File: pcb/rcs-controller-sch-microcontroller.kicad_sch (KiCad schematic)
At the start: 42 parts, among them J11 Conn_01x03, J4 Screw_Terminal_4_P3.50mm, J5 USB_C_Receptacle_USB2.0_14P, J6 Conn_01x03, J9 Conn_01x03, Q2 SI7465DP-T1-E3, Q3 SI7465DP-T1-E3, Q4 PMV45EN2, Q5 PMV45EN2, SW1 SW_Push, SW2 SW_Push, U1 LSM6DSOX, U4 ESP32-S3-WROOM-1

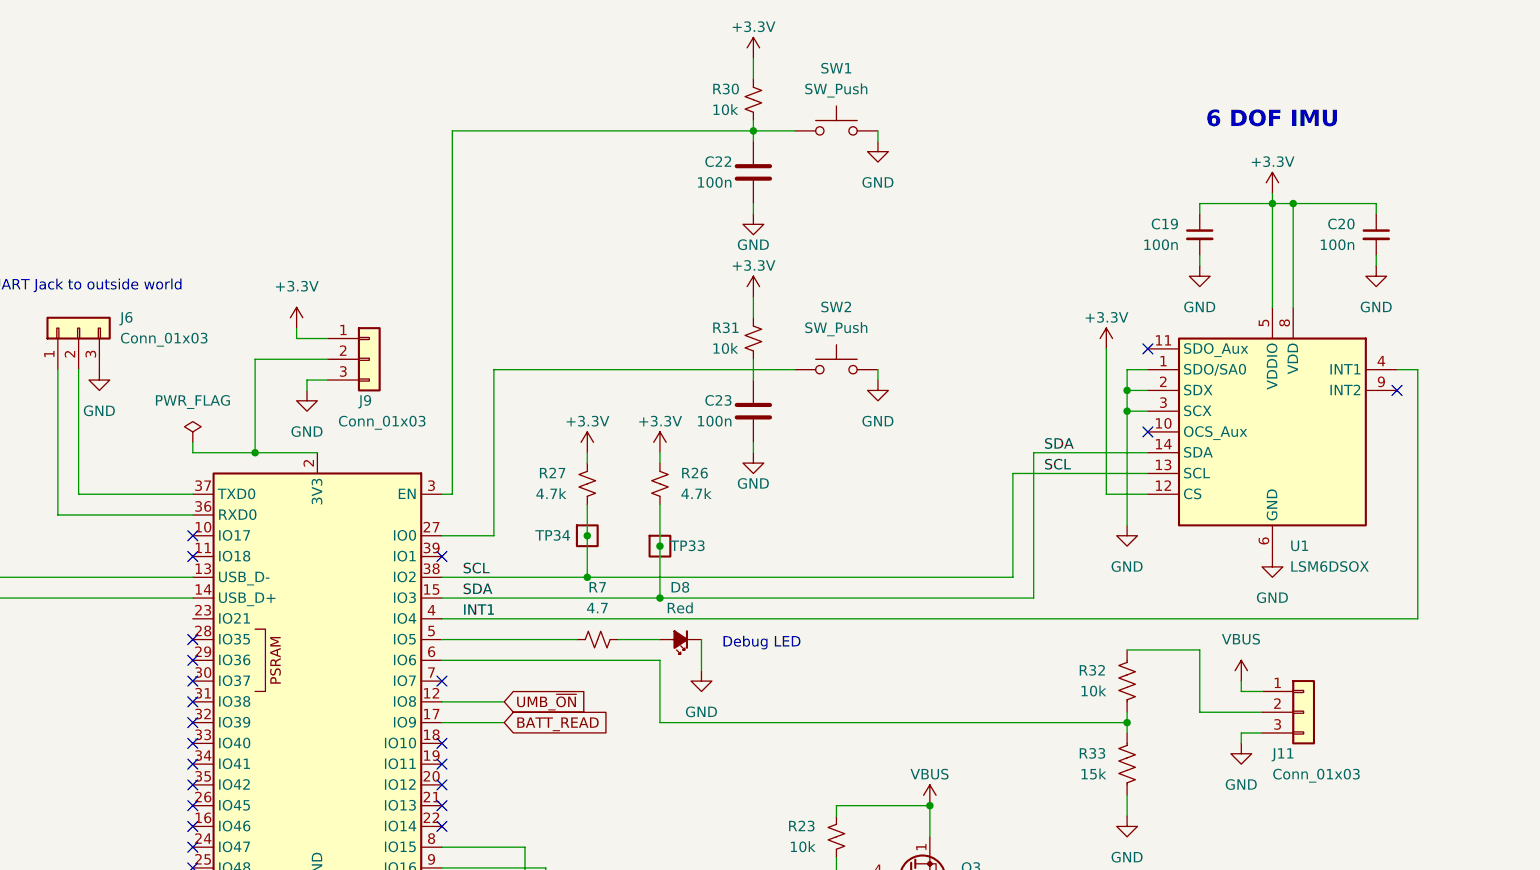
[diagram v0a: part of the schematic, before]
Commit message: Removed CAN stuff and replaced with serial
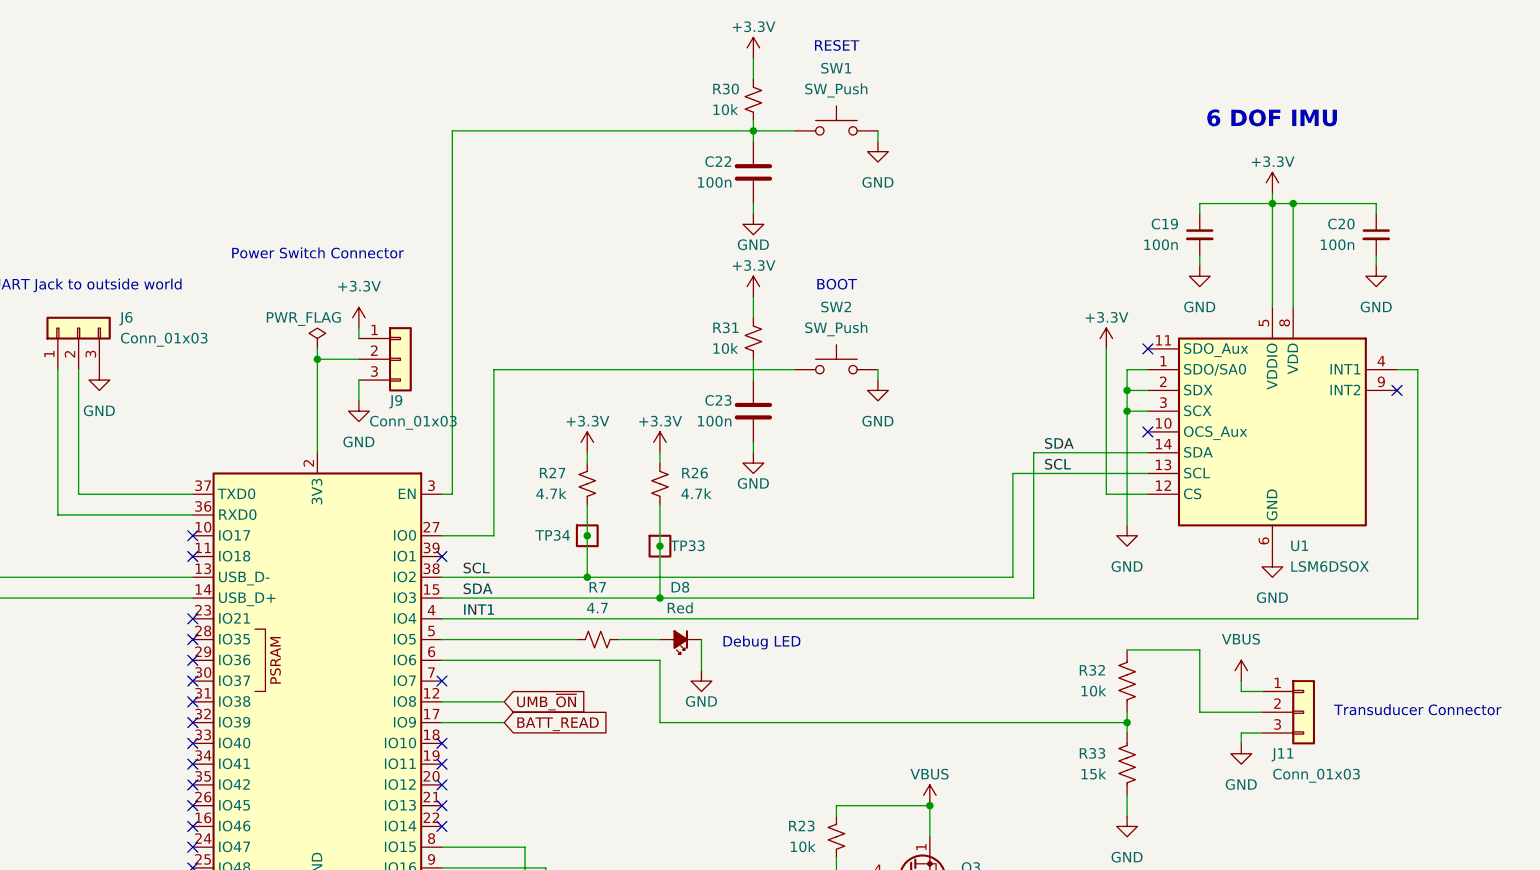
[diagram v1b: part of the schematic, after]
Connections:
- no-connect marks 24 -> 25
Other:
- note added: "BOOT"
- note added: "Power Switch Connector"
- note added: "RESET"
- note added: "Transuducer Connector"
- moved on the sheet: J9
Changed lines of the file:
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@@
 		(rev "1.0")
 	)
+	(text "RESET"
+		(exclude_from_sim no)
+		(at 260.35 58.42 0)
+		(effects
+			(font
+				(size 1.27 1.27)
+			)
+		)
+	)
 	(text "Counter-Clockwise"
 		(exclude_from_sim no)
@@
 		)
 	)
+	(text "BOOT"
+		(exclude_from_sim no)
+		(at 260.35 87.63 0)
+		(effects
+			(font
+				(size 1.27 1.27)
+			)
+		)
+	)
+	(text "Transuducer Connector"
+		(exclude_from_sim no)
+		(at 331.47 139.7 0)
+		(effects
+			(font
+				(size 1.27 1.27)
+			)
+		)
+	)
 	(text "Clockwise\n"
 		(exclude_from_sim no)
@@
 		)
 	)
+	(text "Power Switch Connector"
+		(exclude_from_sim no)
+		(at 196.85 83.82 0)
+		(effects
+			(font
+				(size 1.27 1.27)
+			)
+		)
+	)
 	(text "UART Jack to outside world"
 		(exclude_from_sim no)
@@
 	)
 	(junction
-		(at 189.23 107.95)
-		(diameter 0)
-		(color 0 0 0 0)
-	)
-	(junction
 		(at 271.78 151.13)
 		(diameter 0)
@@
 	)
 	(junction
+		(at 196.85 96.52)
+		(diameter 0)
+		(color 0 0 0 0)
+	)
+	(junction
 		(at 298.45 166.37)
 		(diameter 0)
@@
 	)
 	(no_connect
+		(at 181.61 128.27)
+	)
+	(no_connect
 		(at 181.61 118.11)
 	)
@@
 	(wire
 		(pts
-			(xy 194.31 93.98) (xy 198.12 93.98)
-		)
-		(stroke
-			(width 0)
-			(type default)
-		)
-	)
-	(wire
-		(pts
 			(xy 224.79 158.75) (xy 224.79 171.45)
 		)
@@
 	(wire
 		(pts
-			(xy 196.85 107.95) (xy 189.23 107.95)
-		)
-		(stroke
-			(width 0)
-			(type default)
-		)
-	)
-	(wire
-		(pts
 			(xy 229.87 123.19) (xy 281.94 123.19)
 		)
@@
 	(wire
 		(pts
-			(xy 194.31 92.71) (xy 194.31 93.98)
+			(xy 201.93 92.71) (xy 201.93 93.98)
 		)
 		(stroke
@@
 	(wire
 		(pts
-			(xy 181.61 107.95) (xy 189.23 107.95)
-		)
-		(stroke
-			(width 0)
-			(type default)
-		)
-	)
-	(wire
-		(pts
 			(xy 238.76 133.35) (xy 238.76 140.97)
 		)
@@
 	(wire
 		(pts
-			(xy 195.58 99.06) (xy 195.58 100.33)
+			(xy 201.93 99.06) (xy 201.93 101.6)
 		)
 		(stroke
@@
 	(wire
 		(pts
+			(xy 201.93 96.52) (xy 196.85 96.52)
+		)
+		(stroke
+			(width 0)
+			(type default)
+		)
+	)
+	(wire
+		(pts
 			(xy 102.87 118.11) (xy 123.19 118.11)
 		)
@@
 	(wire
 		(pts
-			(xy 295.91 97.79) (xy 298.45 97.79)
+			(xy 196.85 95.25) (xy 196.85 96.52)
 		)
 		(stroke
@@
 	(wire
 		(pts
-			(xy 260.35 151.13) (xy 260.35 152.4)
+			(xy 295.91 97.79) (xy 298.45 97.79)
 		)
 		(stroke
@@
 	(wire
 		(pts
-			(xy 271.78 165.1) (xy 271.78 166.37)
+			(xy 260.35 151.13) (xy 260.35 152.4)
 		)
 		(stroke
@@
 	(wire
 		(pts
-			(xy 309.88 142.24) (xy 309.88 143.51)
+			(xy 271.78 165.1) (xy 271.78 166.37)
 		)
 		(stroke
@@
 	(wire
 		(pts
-			(xy 189.23 96.52) (xy 189.23 107.95)
+			(xy 309.88 142.24) (xy 309.88 143.51)
 		)
 		(stroke
@@
 	(wire
 		(pts
-			(xy 181.61 106.68) (xy 181.61 107.95)
-		)
-		(stroke
-			(width 0)
-			(type default)
-		)
-	)
-	(wire
-		(pts
 			(xy 295.91 140.97) (xy 295.91 142.24)
 		)
@@
 	(wire
 		(pts
-			(xy 189.23 96.52) (xy 198.12 96.52)
+			(xy 196.85 96.52) (xy 196.85 107.95)
 		)
 		(stroke
@@
 	(wire
 		(pts
-			(xy 198.12 99.06) (xy 195.58 99.06)
-		)
-		(stroke
-			(width 0)
-			(type default)
-		)
-	)
-	(wire
-		(pts
 			(xy 250.19 96.52) (xy 250.19 99.06)
 		)
@@
 	(symbol
 		(lib_id "power:PWR_FLAG")
-		(at 181.61 106.68 0)
+		(at 196.85 95.25 0)
 		(unit 1)
 		(body_style 1)
@@
 		(in_pos_files yes)
 		(dnp no)
-		(fields_autoplaced yes)
 		(property "Reference" "#FLG03"
-			(at 181.61 104.775 0)
+			(at 196.85 93.345 0)
 			(hide yes)
 			(show_name no)
@@
 		)
 		(property "Value" "PWR_FLAG"
-			(at 181.61 101.6 0)
+			(at 190.5 91.44 0)
 			(show_name no)
 			(do_not_autoplace no)
@@
 					(size 1.27 1.27)
 				)
+				(justify left)
 			)
 		)
 		(property "Footprint" ""
-			(at 181.61 106.68 0)
+			(at 196.85 95.25 0)
 			(hide yes)
 			(show_name no)
@@
 		)
 		(property "Datasheet" ""
-			(at 181.61 106.68 0)
+			(at 196.85 95.25 0)
 			(hide yes)
 			(show_name no)
@@
 		)
 		(property "Description" "Special symbol for telling ERC where power comes from"
-			(at 181.61 106.68 0)
+			(at 196.85 95.25 0)
 			(hide yes)
 			(show_name no)
@@
 		(in_pos_files yes)
 		(dnp no)
-		(fields_autoplaced yes)
 		(property "Reference" "#PWR010"
 			(at 243.84 140.97 0)
@@
 		)
 		(property "Value" "GND"
-			(at 243.84 139.7 0)
+			(at 243.84 138.43 0)
 			(show_name no)
 			(do_not_autoplace no)
@@
 	(symbol
 		(lib_id "power:GND")
-		(at 195.58 100.33 0)
+		(at 201.93 101.6 0)
 		(mirror y)
 		(unit 1)
@@
 		(fields_autoplaced yes)
 		(property "Reference" "#PWR066"
-			(at 195.58 106.68 0)
+			(at 201.93 107.95 0)
 			(hide yes)
 			(show_name no)
@@
 		)
 		(property "Value" "GND"
-			(at 195.58 105.41 0)
+			(at 201.93 106.68 0)
 			(show_name no)
 			(do_not_autoplace no)
@@
 		)
 		(property "Footprint" ""
-			(at 195.58 100.33 0)
+			(at 201.93 101.6 0)
 			(hide yes)
 			(show_name no)
@@
 		)
 		(property "Datasheet" ""
-			(at 195.58 100.33 0)
+			(at 201.93 101.6 0)
 			(hide yes)
 			(show_name no)
@@
 		)
 		(property "Description" "Power symbol creates a global label with name \"GND\" , ground"
-			(at 195.58 100.33 0)
+			(at 201.93 101.6 0)
 			(hide yes)
 			(show_name no)
@@
 	(symbol
 		(lib_id "Connector_Generic:Conn_01x03")
-		(at 203.2 96.52 0)
+		(at 207.01 96.52 0)
 		(unit 1)
 		(body_style 1)
@@
 		(dnp no)
 		(property "Reference" "J9"
-			(at 201.93 101.6 0)
+			(at 205.74 101.6 0)
 			(show_name no)
 			(do_not_autoplace no)
@@
 		)
 		(property "Value" "Conn_01x03"
-			(at 199.39 104.14 0)
+			(at 203.2 104.14 0)
 			(show_name no)
 			(do_not_autoplace no)
@@
 		)
 		(property "Footprint" "Connector_Molex:Molex_KK-254_AE-6410-03A_1x03_P2.54mm_Vertical"
-			(at 203.2 96.52 0)
+			(at 207.01 96.52 0)
 			(hide yes)
 			(show_name no)
@@
 		)
 		(property "Datasheet" ""
-			(at 203.2 96.52 0)
+			(at 207.01 96.52 0)
 			(hide yes)
 			(show_name no)
@@
 		)
 		(property "Description" "Generic connector, single row, 01x03, script generated (kicad-library-utils/schlib/autogen/connector/)"
-			(at 203.2 96.52 0)
+			(at 207.01 96.52 0)
 			(hide yes)
 			(show_name no)
@@
 	(symbol
 		(lib_id "power:+3.3V")
-		(at 194.31 92.71 0)
+		(at 201.93 92.71 0)
 		(unit 1)
 		(body_style 1)
@@
 		(fields_autoplaced yes)
 		(property "Reference" "#PWR013"
-			(at 194.31 96.52 0)
+			(at 201.93 96.52 0)
 			(hide yes)
 			(show_name no)
@@
 		)
 		(property "Value" "+3.3V"
-			(at 194.31 87.63 0)
+			(at 201.93 87.63 0)
 			(show_name no)
 			(do_not_autoplace no)
@@
 		)
 		(property "Footprint" ""
-			(at 194.31 92.71 0)
+			(at 201.93 92.71 0)
 			(hide yes)
 			(show_name no)
@@
 		)
 		(property "Datasheet" ""
-			(at 194.31 92.71 0)
+			(at 201.93 92.71 0)
 			(hide yes)
 			(show_name no)
@@
 		)
 		(property "Description" "Power symbol creates a global label with name \"+3.3V\""
-			(at 194.31 92.71 0)
+			(at 201.93 92.71 0)
 			(hide yes)
 			(show_name no)

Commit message: Revert "Removed CAN stuff and replaced with serial"
This reverts commit 91045ad7261f144a15fd34f486a67af6db0fa2f4.
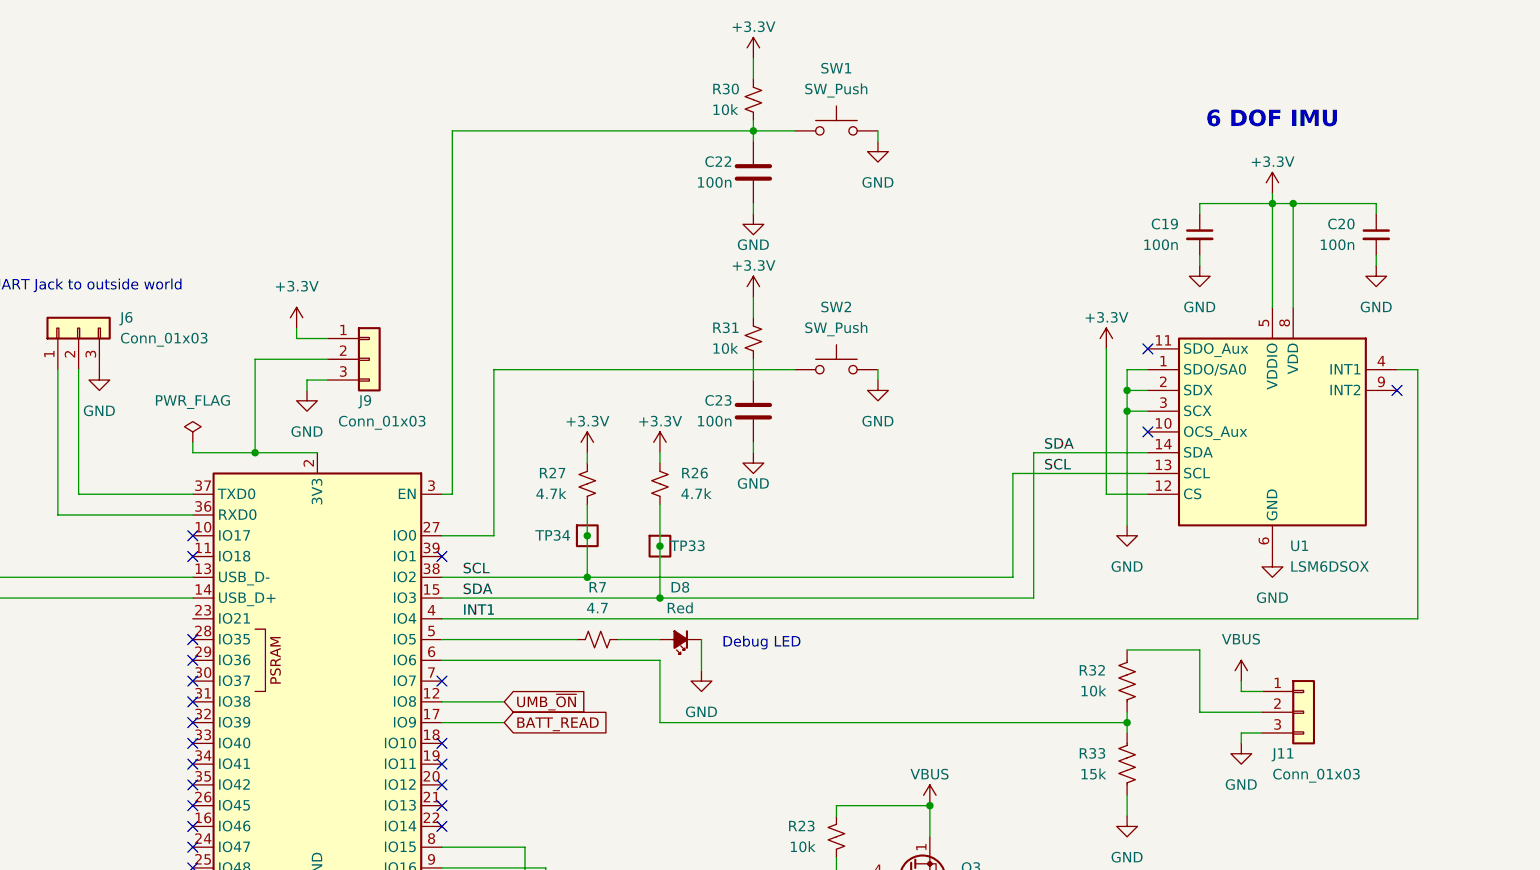
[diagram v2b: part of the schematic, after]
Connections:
- no-connect marks 25 -> 24
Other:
- note removed: "BOOT"
- note removed: "Power Switch Connector"
- note removed: "RESET"
- note removed: "Transuducer Connector"
- moved on the sheet: J9
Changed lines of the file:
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@@
 		(rev "1.0")
 	)
-	(text "RESET"
-		(exclude_from_sim no)
-		(at 260.35 58.42 0)
-		(effects
-			(font
-				(size 1.27 1.27)
-			)
-		)
-	)
 	(text "Counter-Clockwise"
 		(exclude_from_sim no)
@@
 		)
 	)
-	(text "BOOT"
-		(exclude_from_sim no)
-		(at 260.35 87.63 0)
-		(effects
-			(font
-				(size 1.27 1.27)
-			)
-		)
-	)
-	(text "Transuducer Connector"
-		(exclude_from_sim no)
-		(at 331.47 139.7 0)
-		(effects
-			(font
-				(size 1.27 1.27)
-			)
-		)
-	)
 	(text "Clockwise\n"
 		(exclude_from_sim no)
@@
 		)
 	)
-	(text "Power Switch Connector"
-		(exclude_from_sim no)
-		(at 196.85 83.82 0)
-		(effects
-			(font
-				(size 1.27 1.27)
-			)
-		)
-	)
 	(text "UART Jack to outside world"
 		(exclude_from_sim no)
@@
 	)
 	(junction
-		(at 271.78 151.13)
+		(at 189.23 107.95)
 		(diameter 0)
 		(color 0 0 0 0)
 	)
 	(junction
-		(at 261.62 204.47)
+		(at 271.78 151.13)
 		(diameter 0)
 		(color 0 0 0 0)
 	)
 	(junction
-		(at 295.91 102.87)
+		(at 261.62 204.47)
 		(diameter 0)
 		(color 0 0 0 0)
 	)
 	(junction
-		(at 295.91 210.82)
+		(at 295.91 102.87)
 		(diameter 0)
 		(color 0 0 0 0)
 	)
 	(junction
-		(at 196.85 96.52)
+		(at 295.91 210.82)
 		(diameter 0)
 		(color 0 0 0 0)
@@
 	)
 	(no_connect
-		(at 181.61 128.27)
-	)
-	(no_connect
 		(at 181.61 118.11)
 	)
@@
 	(wire
 		(pts
+			(xy 194.31 93.98) (xy 198.12 93.98)
+		)
+		(stroke
+			(width 0)
+			(type default)
+		)
+	)
+	(wire
+		(pts
 			(xy 224.79 158.75) (xy 224.79 171.45)
 		)
@@
 	(wire
 		(pts
+			(xy 196.85 107.95) (xy 189.23 107.95)
+		)
+		(stroke
+			(width 0)
+			(type default)
+		)
+	)
+	(wire
+		(pts
 			(xy 229.87 123.19) (xy 281.94 123.19)
 		)
@@
 	(wire
 		(pts
-			(xy 201.93 92.71) (xy 201.93 93.98)
+			(xy 194.31 92.71) (xy 194.31 93.98)
 		)
 		(stroke
@@
 	(wire
 		(pts
+			(xy 181.61 107.95) (xy 189.23 107.95)
+		)
+		(stroke
+			(width 0)
+			(type default)
+		)
+	)
+	(wire
+		(pts
 			(xy 238.76 133.35) (xy 238.76 140.97)
 		)
@@
 	(wire
 		(pts
-			(xy 201.93 99.06) (xy 201.93 101.6)
+			(xy 195.58 99.06) (xy 195.58 100.33)
 		)
 		(stroke
@@
 	(wire
 		(pts
-			(xy 201.93 96.52) (xy 196.85 96.52)
-		)
-		(stroke
-			(width 0)
-			(type default)
-		)
-	)
-	(wire
-		(pts
 			(xy 102.87 118.11) (xy 123.19 118.11)
 		)
@@
 	(wire
 		(pts
-			(xy 196.85 95.25) (xy 196.85 96.52)
+			(xy 295.91 97.79) (xy 298.45 97.79)
 		)
 		(stroke
@@
 	(wire
 		(pts
-			(xy 295.91 97.79) (xy 298.45 97.79)
+			(xy 260.35 151.13) (xy 260.35 152.4)
 		)
 		(stroke
@@
 	(wire
 		(pts
-			(xy 260.35 151.13) (xy 260.35 152.4)
+			(xy 271.78 165.1) (xy 271.78 166.37)
 		)
 		(stroke
@@
 	(wire
 		(pts
-			(xy 271.78 165.1) (xy 271.78 166.37)
+			(xy 309.88 142.24) (xy 309.88 143.51)
 		)
 		(stroke
@@
 	(wire
 		(pts
-			(xy 309.88 142.24) (xy 309.88 143.51)
+			(xy 189.23 96.52) (xy 189.23 107.95)
 		)
 		(stroke
@@
 	(wire
 		(pts
+			(xy 181.61 106.68) (xy 181.61 107.95)
+		)
+		(stroke
+			(width 0)
+			(type default)
+		)
+	)
+	(wire
+		(pts
 			(xy 295.91 140.97) (xy 295.91 142.24)
 		)
@@
 	(wire
 		(pts
-			(xy 196.85 96.52) (xy 196.85 107.95)
+			(xy 189.23 96.52) (xy 198.12 96.52)
 		)
 		(stroke
@@
 	(wire
 		(pts
+			(xy 198.12 99.06) (xy 195.58 99.06)
+		)
+		(stroke
+			(width 0)
+			(type default)
+		)
+	)
+	(wire
+		(pts
 			(xy 250.19 96.52) (xy 250.19 99.06)
 		)
@@
 	(symbol
 		(lib_id "power:PWR_FLAG")
-		(at 196.85 95.25 0)
+		(at 181.61 106.68 0)
 		(unit 1)
 		(body_style 1)
@@
 		(in_pos_files yes)
 		(dnp no)
+		(fields_autoplaced yes)
 		(property "Reference" "#FLG03"
-			(at 196.85 93.345 0)
+			(at 181.61 104.775 0)
 			(hide yes)
 			(show_name no)
@@
 		)
 		(property "Value" "PWR_FLAG"
-			(at 190.5 91.44 0)
+			(at 181.61 101.6 0)
 			(show_name no)
 			(do_not_autoplace no)
@@
 					(size 1.27 1.27)
 				)
-				(justify left)
 			)
 		)
 		(property "Footprint" ""
-			(at 196.85 95.25 0)
+			(at 181.61 106.68 0)
 			(hide yes)
 			(show_name no)
@@
 		)
 		(property "Datasheet" ""
-			(at 196.85 95.25 0)
+			(at 181.61 106.68 0)
 			(hide yes)
 			(show_name no)
@@
 		)
 		(property "Description" "Special symbol for telling ERC where power comes from"
-			(at 196.85 95.25 0)
+			(at 181.61 106.68 0)
 			(hide yes)
 			(show_name no)
@@
 		(in_pos_files yes)
 		(dnp no)
+		(fields_autoplaced yes)
 		(property "Reference" "#PWR010"
 			(at 243.84 140.97 0)
@@
 		)
 		(property "Value" "GND"
-			(at 243.84 138.43 0)
+			(at 243.84 139.7 0)
 			(show_name no)
 			(do_not_autoplace no)
@@
 	(symbol
 		(lib_id "power:GND")
-		(at 201.93 101.6 0)
+		(at 195.58 100.33 0)
 		(mirror y)
 		(unit 1)
@@
 		(fields_autoplaced yes)
 		(property "Reference" "#PWR066"
-			(at 201.93 107.95 0)
+			(at 195.58 106.68 0)
 			(hide yes)
 			(show_name no)
@@
 		)
 		(property "Value" "GND"
-			(at 201.93 106.68 0)
+			(at 195.58 105.41 0)
 			(show_name no)
 			(do_not_autoplace no)
@@
 		)
 		(property "Footprint" ""
-			(at 201.93 101.6 0)
+			(at 195.58 100.33 0)
 			(hide yes)
 			(show_name no)
@@
 		)
 		(property "Datasheet" ""
-			(at 201.93 101.6 0)
+			(at 195.58 100.33 0)
 			(hide yes)
 			(show_name no)
@@
 		)
 		(property "Description" "Power symbol creates a global label with name \"GND\" , ground"
-			(at 201.93 101.6 0)
+			(at 195.58 100.33 0)
 			(hide yes)
 			(show_name no)
@@
 	(symbol
 		(lib_id "Connector_Generic:Conn_01x03")
-		(at 207.01 96.52 0)
+		(at 203.2 96.52 0)
 		(unit 1)
 		(body_style 1)
@@
 		(dnp no)
 		(property "Reference" "J9"
-			(at 205.74 101.6 0)
+			(at 201.93 101.6 0)
 			(show_name no)
 			(do_not_autoplace no)
@@
 		)
 		(property "Value" "Conn_01x03"
-			(at 203.2 104.14 0)
+			(at 199.39 104.14 0)
 			(show_name no)
 			(do_not_autoplace no)
@@
 		)
 		(property "Footprint" "Connector_Molex:Molex_KK-254_AE-6410-03A_1x03_P2.54mm_Vertical"
-			(at 207.01 96.52 0)
+			(at 203.2 96.52 0)
 			(hide yes)
 			(show_name no)
@@
 		)
 		(property "Datasheet" ""
-			(at 207.01 96.52 0)
+			(at 203.2 96.52 0)
 			(hide yes)
 			(show_name no)
@@
 		)
 		(property "Description" "Generic connector, single row, 01x03, script generated (kicad-library-utils/schlib/autogen/connector/)"
-			(at 207.01 96.52 0)
+			(at 203.2 96.52 0)
 			(hide yes)
 			(show_name no)
@@
 	(symbol
 		(lib_id "power:+3.3V")
-		(at 201.93 92.71 0)
+		(at 194.31 92.71 0)
 		(unit 1)
 		(body_style 1)
@@
 		(fields_autoplaced yes)
 		(property "Reference" "#PWR013"
-			(at 201.93 96.52 0)
+			(at 194.31 96.52 0)
 			(hide yes)
 			(show_name no)
@@
 		)
 		(property "Value" "+3.3V"
-			(at 201.93 87.63 0)
+			(at 194.31 87.63 0)
 			(show_name no)
 			(do_not_autoplace no)
@@
 		)
 		(property "Footprint" ""
-			(at 201.93 92.71 0)
+			(at 194.31 92.71 0)
 			(hide yes)
 			(show_name no)
@@
 		)
 		(property "Datasheet" ""
-			(at 201.93 92.71 0)
+			(at 194.31 92.71 0)
 			(hide yes)
 			(show_name no)
@@
 		)
 		(property "Description" "Power symbol creates a global label with name \"+3.3V\""
-			(at 201.93 92.71 0)
+			(at 194.31 92.71 0)
 			(hide yes)
 			(show_name no)
